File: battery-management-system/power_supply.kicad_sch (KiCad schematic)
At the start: 49 parts, among them J14 -5V, J24 3V3, J25 5V, J26 18V, J28 9V4, U1 L6982C33DR, U12 ICL7660, U15 ICL7660, U16 ICL7660, U2 L6982C33DR

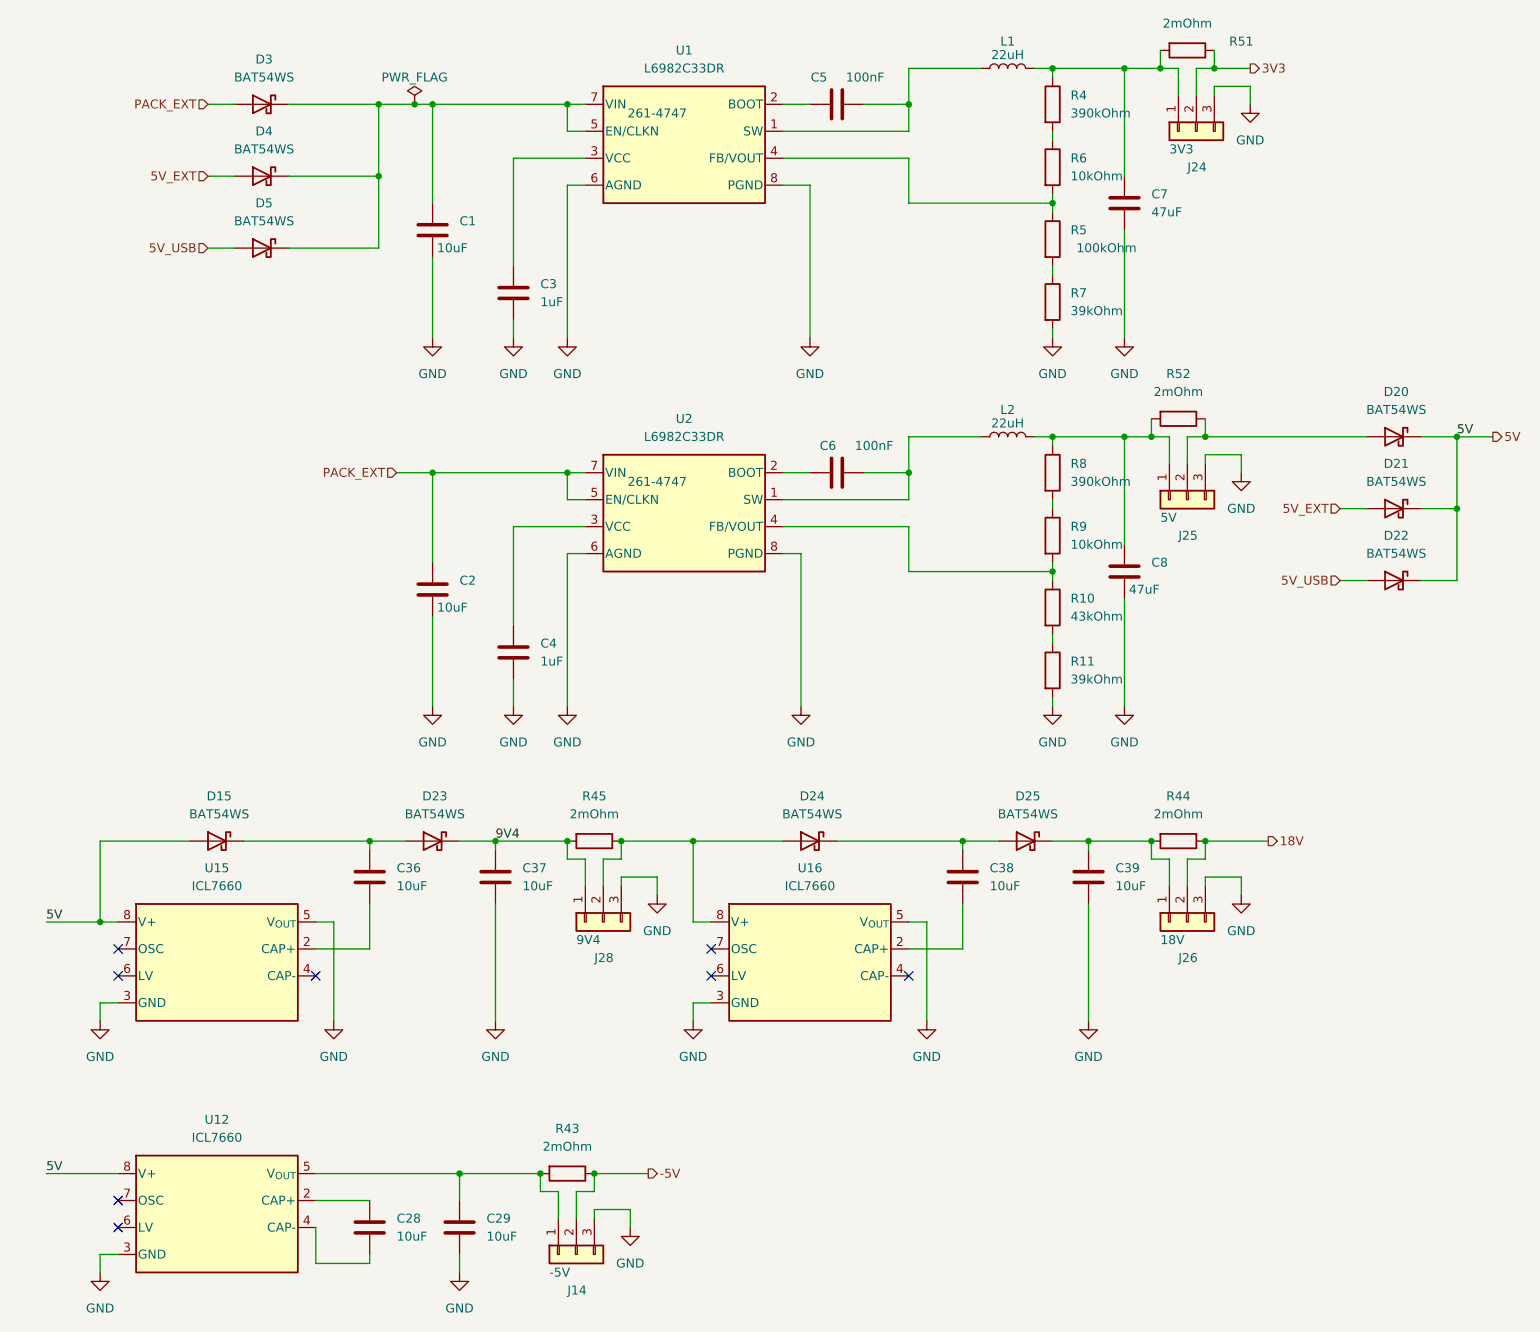
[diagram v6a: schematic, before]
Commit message: fix ERC issues
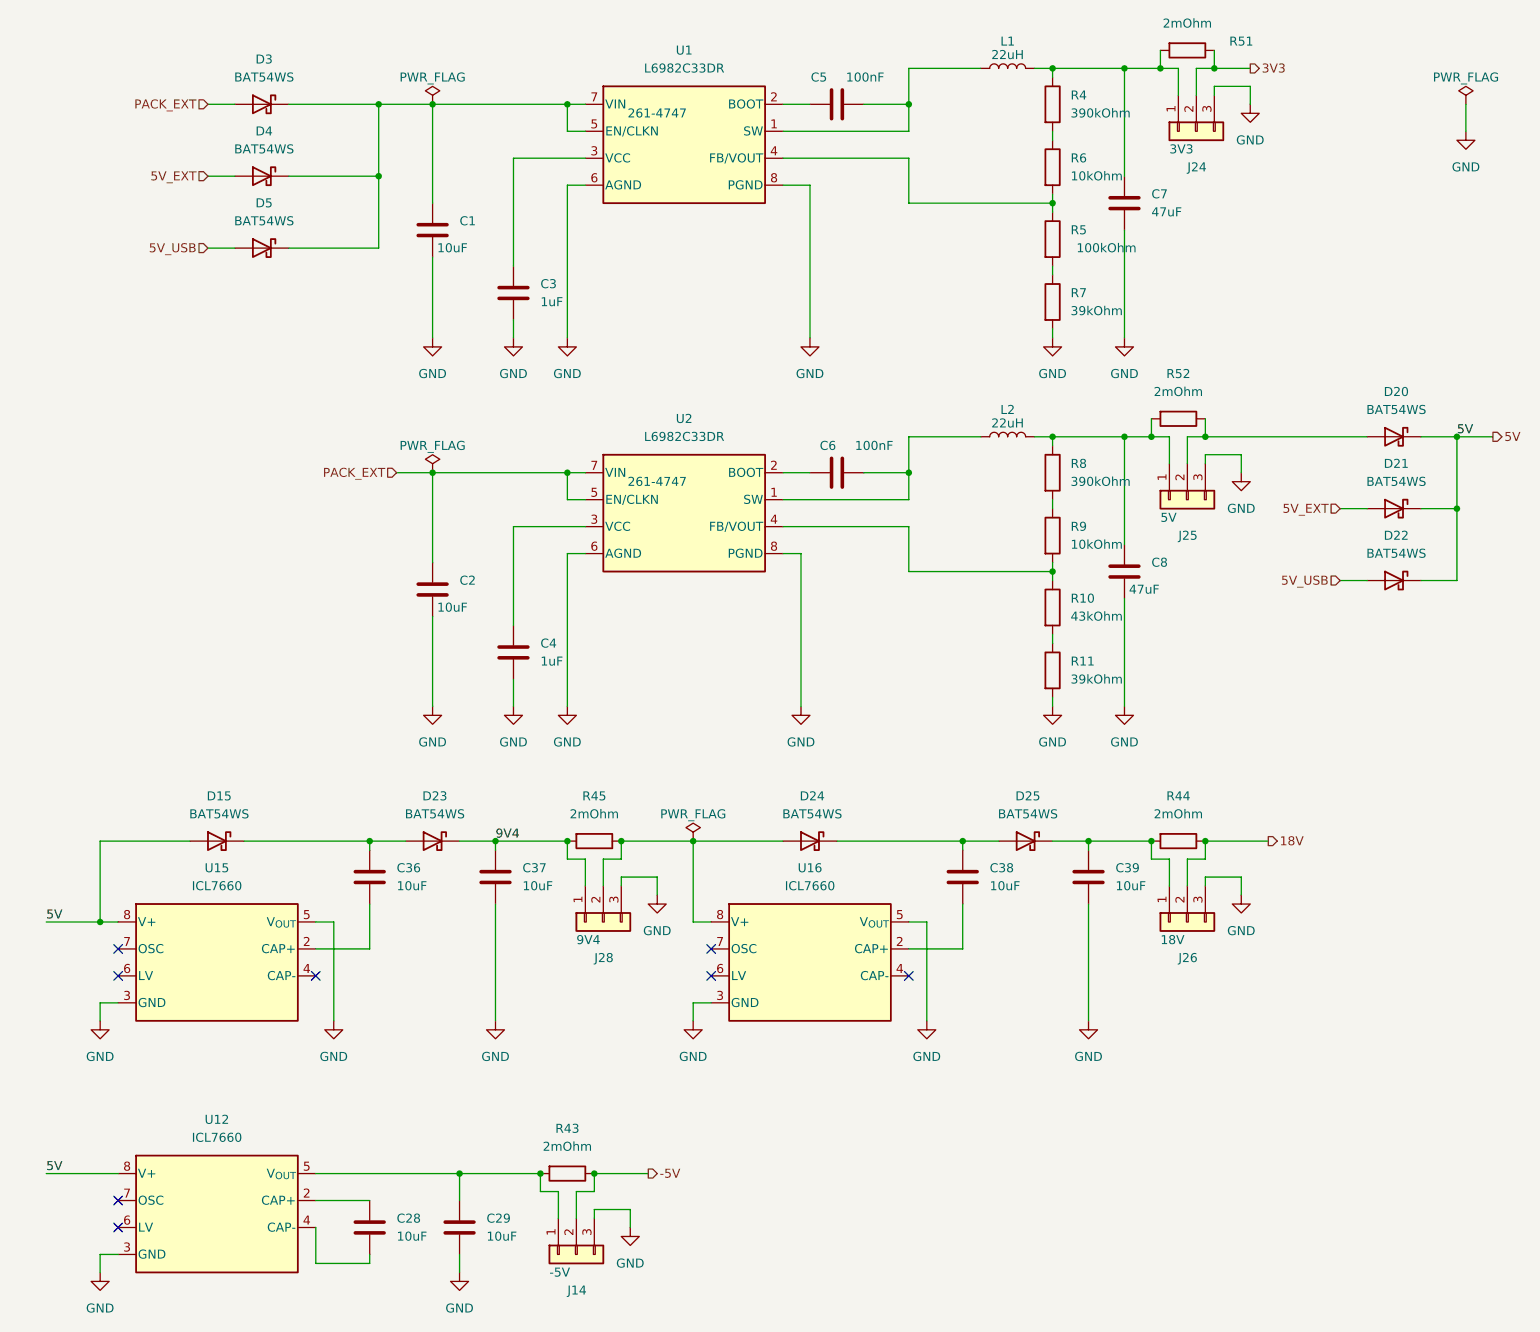
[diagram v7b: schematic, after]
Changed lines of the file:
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@@
   (junction (at 185.42 20.32) (diameter 0) (color 0 0 0 0)
-  )
-  (junction (at 72.39 25.4) (diameter 0) (color 0 0 0 0)
   )
   (junction (at 111.76 129.54) (diameter 0) (color 0 0 0 0)
@@
     (stroke (width 0) (type default))
   )
+  (wire (pts (xy 220.98 25.4) (xy 220.98 29.21))
+    (stroke (width 0) (type default))
+  )
   (wire (pts (xy 124.46 81.28) (xy 142.24 81.28))
     (stroke (width 0) (type default))
@@
     (stroke (width 0) (type default))
   )
-  (wire (pts (xy 72.39 25.4) (xy 67.31 25.4))
+  (wire (pts (xy 67.31 25.4) (xy 74.93 25.4))
     (stroke (width 0) (type default))
   )
@@
     (stroke (width 0) (type default))
   )
-  (wire (pts (xy 74.93 25.4) (xy 72.39 25.4))
-    (stroke (width 0) (type default))
-  )
   (wire (pts (xy 185.42 22.86) (xy 185.42 24.13))
     (stroke (width 0) (type default))
@@
     (stroke (width 0) (type default))
   )
-  (wire (pts (xy 74.93 77.47) (xy 69.85 77.47))
+  (wire (pts (xy 69.85 77.47) (xy 74.93 77.47))
     (stroke (width 0) (type default))
   )
@@
     )
   )
+  (symbol (lib_id "power:PWR_FLAG") (at 220.98 25.4 0) (unit 1)
+    (in_bom yes) (on_board yes) (dnp no)
+    (property "Reference" "#FLG010" (at 220.98 23.495 0)
+      (effects (font (size 1.27 1.27)) hide)
+    )
+    (property "Value" "PWR_FLAG" (at 220.98 21.59 0)
+      (effects (font (size 1.27 1.27)))
+    )
+    (property "Footprint" "" (at 220.98 25.4 0)
+      (effects (font (size 1.27 1.27)) hide)
+    )
+    (property "Datasheet" "~" (at 220.98 25.4 0)
+      (effects (font (size 1.27 1.27)) hide)
+    )
+    (pin "1")
+    (instances
+      (project "battery-management-system"
+        (path "/5272f0ff-3069-41a9-bca2-80beede8b4b2/b1377397-46a1-4623-af59-88e4e694ca35"
+          (reference "#FLG010") (unit 1)
+        )
+      )
+    )
+  )
   (symbol (lib_id "power:GND") (at 93.98 58.42 0) (unit 1)
     (in_bom yes) (on_board yes) (dnp no) (fields_autoplaced)
@@
     )
   )
+  (symbol (lib_id "power:PWR_FLAG") (at 111.76 129.54 0) (unit 1)
+    (in_bom yes) (on_board yes) (dnp no)
+    (property "Reference" "#FLG08" (at 111.76 127.635 0)
+      (effects (font (size 1.27 1.27)) hide)
+    )
+    (property "Value" "PWR_FLAG" (at 111.76 125.73 0)
+      (effects (font (size 1.27 1.27)))
+    )
+    (property "Footprint" "" (at 111.76 129.54 0)
+      (effects (font (size 1.27 1.27)) hide)
+    )
+    (property "Datasheet" "~" (at 111.76 129.54 0)
+      (effects (font (size 1.27 1.27)) hide)
+    )
+    (pin "1")
+    (instances
+      (project "battery-management-system"
+        (path "/5272f0ff-3069-41a9-bca2-80beede8b4b2/b1377397-46a1-4623-af59-88e4e694ca35"
+          (reference "#FLG08") (unit 1)
+        )
+      )
+    )
+  )
   (symbol (lib_id "benediktibk:R_2mOhm_SMD_2512_5W_1%") (at 181.61 17.78 270) (unit 1)
     (in_bom yes) (on_board yes) (dnp no)
@@
     )
   )
-  (symbol (lib_id "power:PWR_FLAG") (at 72.39 25.4 0) (unit 1)
+  (symbol (lib_id "power:PWR_FLAG") (at 74.93 25.4 0) (unit 1)
     (in_bom yes) (on_board yes) (dnp no)
-    (property "Reference" "#FLG01" (at 72.39 23.495 0)
-      (effects (font (size 1.27 1.27)) hide)
-    )
-    (property "Value" "PWR_FLAG" (at 72.39 21.59 0)
-      (effects (font (size 1.27 1.27)))
-    )
-    (property "Footprint" "" (at 72.39 25.4 0)
-      (effects (font (size 1.27 1.27)) hide)
-    )
-    (property "Datasheet" "~" (at 72.39 25.4 0)
+    (property "Reference" "#FLG01" (at 74.93 23.495 0)
+      (effects (font (size 1.27 1.27)) hide)
+    )
+    (property "Value" "PWR_FLAG" (at 74.93 21.59 0)
+      (effects (font (size 1.27 1.27)))
+    )
+    (property "Footprint" "" (at 74.93 25.4 0)
+      (effects (font (size 1.27 1.27)) hide)
+    )
+    (property "Datasheet" "~" (at 74.93 25.4 0)
       (effects (font (size 1.27 1.27)) hide)
     )
@@
     )
   )
+  (symbol (lib_id "power:GND") (at 220.98 29.21 0) (unit 1)
+    (in_bom yes) (on_board yes) (dnp no) (fields_autoplaced)
+    (property "Reference" "#PWR042" (at 220.98 35.56 0)
+      (effects (font (size 1.27 1.27)) hide)
+    )
+    (property "Value" "GND" (at 220.98 34.29 0)
+      (effects (font (size 1.27 1.27)))
+    )
+    (property "Footprint" "" (at 220.98 29.21 0)
+      (effects (font (size 1.27 1.27)) hide)
+    )
+    (property "Datasheet" "" (at 220.98 29.21 0)
+      (effects (font (size 1.27 1.27)) hide)
+    )
+    (pin "1")
+    (instances
+      (project "battery-management-system"
+        (path "/5272f0ff-3069-41a9-bca2-80beede8b4b2/b1377397-46a1-4623-af59-88e4e694ca35"
+          (reference "#PWR042") (unit 1)
+        )
+      )
+    )
+  )
   (symbol (lib_id "benediktibk:R_2mOhm_SMD_2512_5W_1%") (at 97.79 129.54 270) (unit 1)
     (in_bom yes) (on_board yes) (dnp no)
@@
         )
       )
+    )
+  )
+  (symbol (lib_id "power:PWR_FLAG") (at 74.93 77.47 0) (unit 1)
+    (in_bom yes) (on_board yes) (dnp no)
+    (property "Reference" "#FLG04" (at 74.93 75.565 0)
+      (effects (font (size 1.27 1.27)) hide)
+    )
+    (property "Value" "PWR_FLAG" (at 74.93 73.66 0)
+      (effects (font (size 1.27 1.27)))
+    )
+    (property "Footprint" "" (at 74.93 77.47 0)
+      (effects (font (size 1.27 1.27)) hide)
+    )
+    (property "Datasheet" "~" (at 74.93 77.47 0)
+      (effects (font (size 1.27 1.27)) hide)
+    )
+    (pin "1")
+    (instances
+      (project "battery-management-system"
+        (path "/5272f0ff-3069-41a9-bca2-80beede8b4b2/b1377397-46a1-4623-af59-88e4e694ca35"
+          (reference "#FLG04") (unit 1)
+        )
+      )

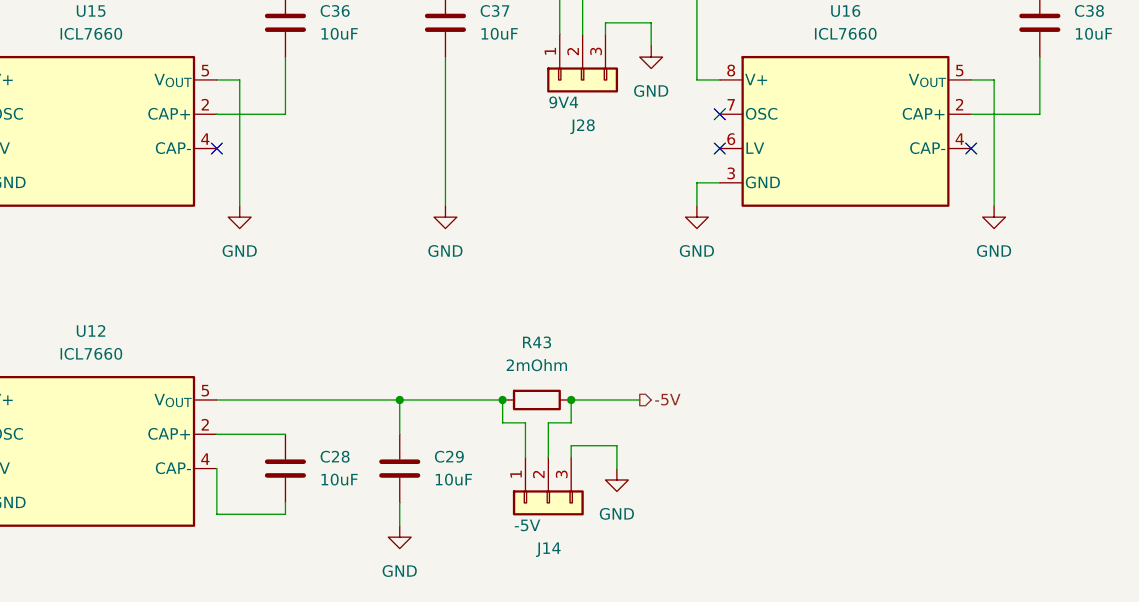
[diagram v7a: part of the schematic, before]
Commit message: fix PCB errors
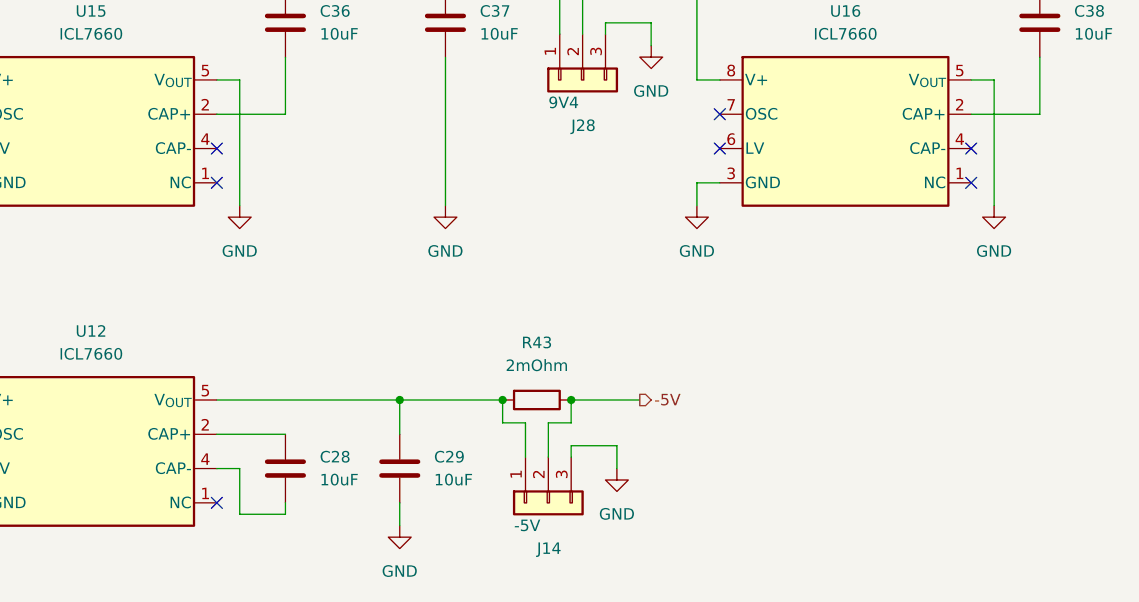
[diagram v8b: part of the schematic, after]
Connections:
- no-connect marks 8 -> 11
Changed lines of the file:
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@@
   (no_connect (at 142.24 148.59))
   (no_connect (at 30.48 148.59))
+  (no_connect (at 142.24 152.4))
+  (no_connect (at 58.42 187.96))
   (no_connect (at 114.3 144.78))
   (no_connect (at 30.48 184.15))
@@
   (no_connect (at 30.48 180.34))
   (no_connect (at 30.48 144.78))
+  (no_connect (at 58.42 152.4))
   (no_connect (at 58.42 148.59))
+  (wire (pts (xy 60.96 184.15) (xy 60.96 189.23))
+    (stroke (width 0) (type default))
+  )
   (wire (pts (xy 66.04 130.81) (xy 66.04 129.54))
     (stroke (width 0) (type default))
@@
     (stroke (width 0) (type default))
   )
+  (wire (pts (xy 60.96 184.15) (xy 58.42 184.15))
+    (stroke (width 0) (type default))
+  )
   (wire (pts (xy 162.56 91.44) (xy 162.56 90.17))
     (stroke (width 0) (type default))
@@
     (stroke (width 0) (type default))
   )
+  (wire (pts (xy 60.96 189.23) (xy 66.04 189.23))
+    (stroke (width 0) (type default))
+  )
   (wire (pts (xy 162.56 109.22) (xy 162.56 110.49))
     (stroke (width 0) (type default))
@@
     (stroke (width 0) (type default))
   )
-  (wire (pts (xy 66.04 189.23) (xy 58.42 189.23))
-    (stroke (width 0) (type default))
-  )
   (wire (pts (xy 142.24 85.09) (xy 142.24 91.44))
     (stroke (width 0) (type default))
@@
   )
   (wire (pts (xy 184.15 134.62) (xy 184.15 135.89))
-    (stroke (width 0) (type default))
-  )
-  (wire (pts (xy 58.42 189.23) (xy 58.42 184.15))
     (stroke (width 0) (type default))
   )
@@
     (pin "4")
     (pin "2")
+    (pin "1")
     (instances
       (project "battery-management-system"
@@
     (pin "4")
     (pin "2")
+    (pin "1")
     (instances
       (project "battery-management-system"
@@
     (pin "4")
     (pin "2")
-    (instances
-      (project "battery-management-system"
+    (pin "1")
+    (instances
+      (project "battery-management-system"
